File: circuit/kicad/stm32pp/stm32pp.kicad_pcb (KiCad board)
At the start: 2 copper layers, 59.8 x 34.2 mm, 30 parts, among them J1 USB_B_Micro, J2 USB_B_Micro, J3 Conn_01x04_Male, J4 Conn_01x08_Male, J5 Conn_01x08_Male, J6 Conn_01x08_Male, J7 Conn_01x08_Male, J8 Conn_01x02_Male, SW1 SW_Push, SW2 SW_Push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

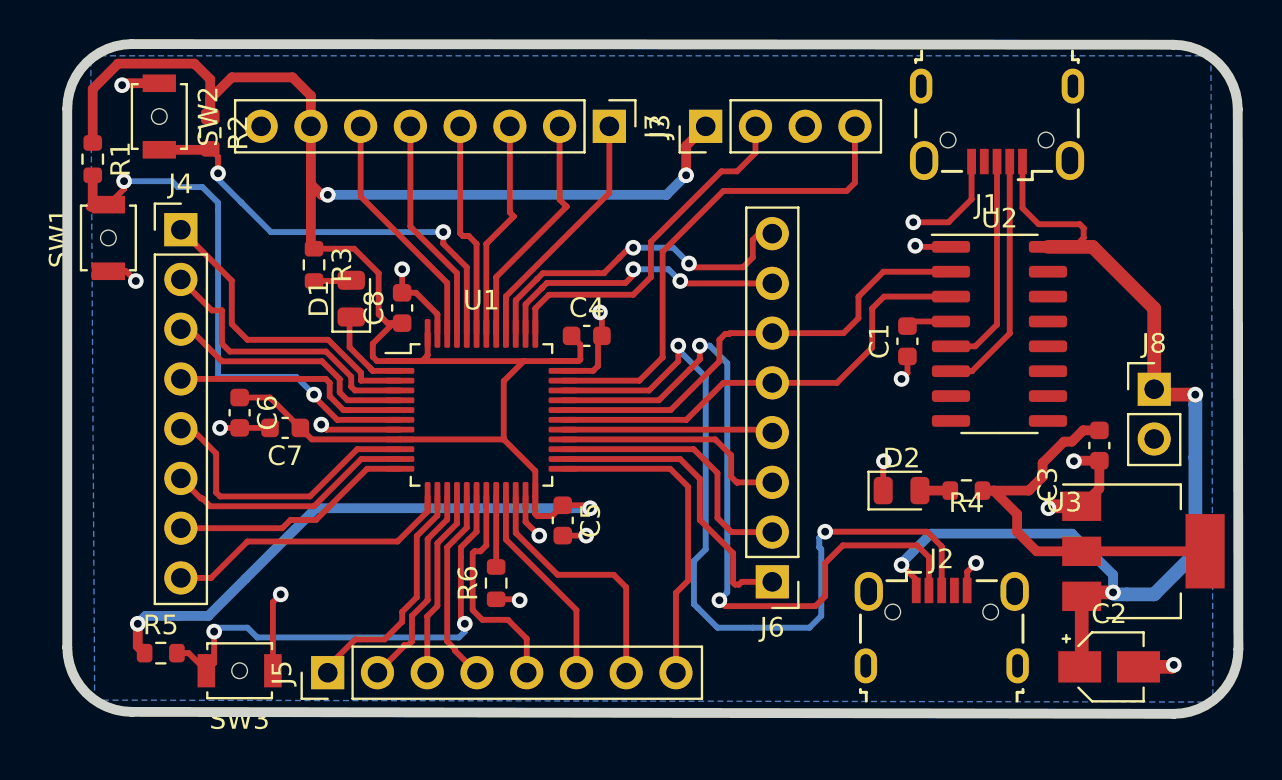
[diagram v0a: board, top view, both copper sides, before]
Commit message: STM32 PP
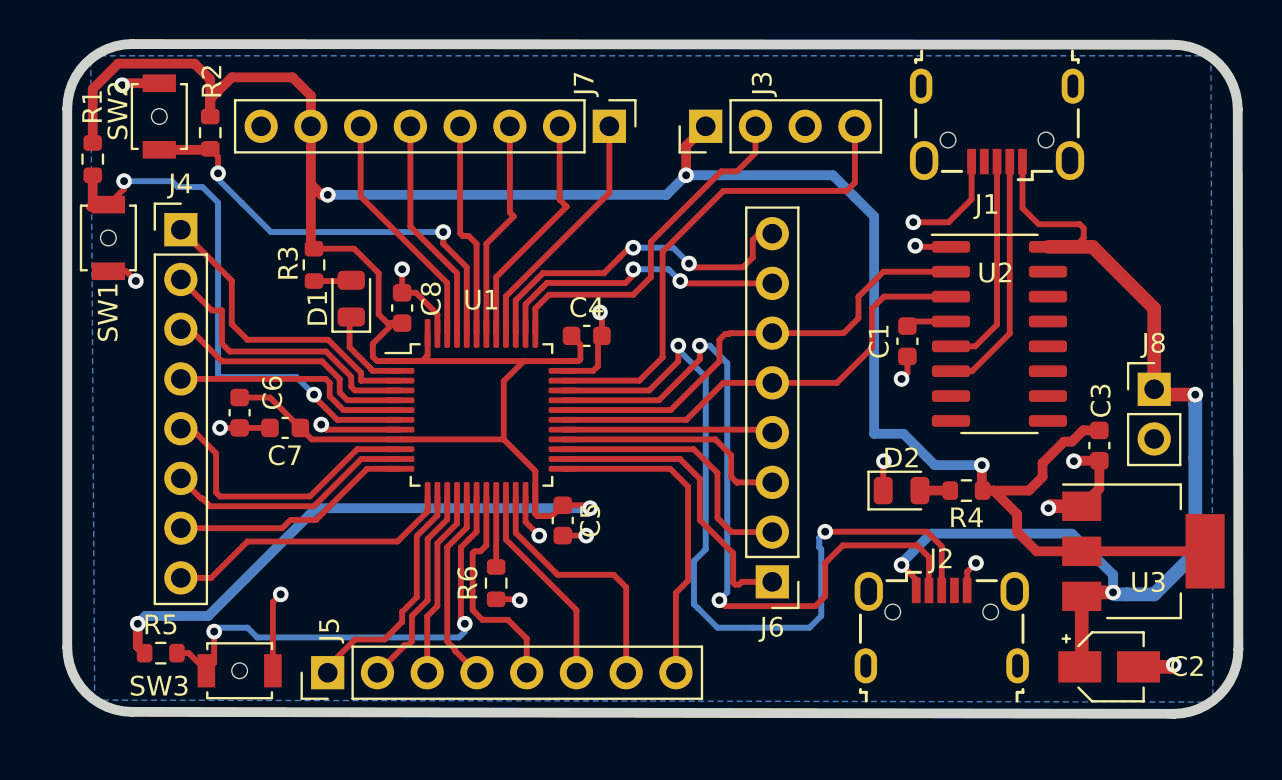
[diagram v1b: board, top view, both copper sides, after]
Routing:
- net +3.3V: track 146.6 -> 175.7 mm, vias 4 -> 5
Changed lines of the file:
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@@
     (property "Sheetname" "")
     (attr smd)
-    (fp_text reference "SW1" (at 0 -2.5 90) (layer "F.SilkS")
+    (fp_text reference "SW1" (at -3.8 0 90) (layer "F.SilkS")
       (effects (font (size 1 1) (thickness 0.15)))
     )
@@
     (property "Sheetname" "")
     (attr through_hole)
-    (fp_text reference "J7" (at 0 -2.33 90) (layer "F.SilkS")
+    (fp_text reference "J7" (at -2.2 1.28 90) (layer "F.SilkS")
       (effects (font (size 1 1) (thickness 0.15)))
     )
@@
     (property "Sheetname" "")
     (attr smd)
-    (fp_text reference "R3" (at 0 -1.43 90) (layer "F.SilkS")
+    (fp_text reference "R3" (at -0.075 1.3 90) (layer "F.SilkS")
       (effects (font (size 1 1) (thickness 0.15)))
     )
@@
     (property "Sheetname" "")
     (attr smd)
-    (fp_text reference "R2" (at 0 -1.43 90) (layer "F.SilkS")
+    (fp_text reference "R2" (at -2.625 -0.1 90) (layer "F.SilkS")
       (effects (font (size 1 1) (thickness 0.15)))
     )
@@
     (property "Sheetname" "")
     (attr smd)
-    (fp_text reference "C3" (at 2 2.6325 90) (layer "F.SilkS")
+    (fp_text reference "C3" (at -2.3 -0.1 90) (layer "F.SilkS")
       (effects (font (size 1 1) (thickness 0.15)))
     )
@@
     (pad "6" thru_hole oval (at 3.725 -1.85 180) (size 1.45 2) (drill oval 0.85 1.4) (layers *.Cu *.Mask)
       (net 1 "GND") (pinfunction "Shield") (pintype "passive"))
-    (model "${KICAD6_3DMODEL_DIR}/Connector_USB.3dshapes/USB_Micro-B_Wuerth_629105150521.wrl"
-      (offset (xyz 0 0 0))
-      (scale (xyz 1 1 1))
-      (rotate (xyz 0 0 0))
+    (model "${KIPRJMOD}/libs/pkg3d/molex_0473460001.stp"
+      (offset (xyz 0 -1.2 0))
+      (scale (xyz 1 1 1))
+      (rotate (xyz -90 0 0))
     )
   )
@@
     (property "Sheetname" "")
     (attr through_hole)
-    (fp_text reference "J3" (at 0 -2.33 90) (layer "F.SilkS")
+    (fp_text reference "J3" (at 2.2 2.9 90) (layer "F.SilkS")
       (effects (font (size 1 1) (thickness 0.15)))
     )
@@
     (property "Sheetname" "")
     (attr smd)
-    (fp_text reference "U3" (at -4.0625 -2.5) (layer "F.SilkS")
+    (fp_text reference "U3" (at 0.25 1.6) (layer "F.SilkS")
       (effects (font (size 1 1) (thickness 0.15)))
     )
@@
     (property "Sheetname" "")
     (attr smd)
-    (fp_text reference "R4" (at 0 -0.63) (layer "F.SilkS")
+    (fp_text reference "R4" (at 0 -1.4) (layer "F.SilkS")
       (effects (font (size 1 1) (thickness 0.15)))
     )
@@
     (property "Sheetname" "")
     (attr through_hole)
-    (fp_text reference "J5" (at 0 -2.33 90) (layer "F.SilkS")
+    (fp_text reference "J5" (at 2.2 0.1 90) (layer "F.SilkS")
       (effects (font (size 1 1) (thickness 0.15)))
     )
@@
     (property "Sheetname" "")
     (attr smd)
-    (fp_text reference "C2" (at 0 -2.7) (layer "F.SilkS")
+    (fp_text reference "C2" (at 4 0) (layer "F.SilkS")
       (effects (font (size 1 1) (thickness 0.15)))
     )
@@
     (property "Sheetname" "")
     (attr smd)
-    (fp_text reference "C6" (at 0 -1.43 90) (layer "F.SilkS")
+    (fp_text reference "C6" (at -1.025 -1.7 90) (layer "F.SilkS")
       (effects (font (size 1 1) (thickness 0.15)))
     )
@@
     (property "Sheetname" "")
     (attr smd)
-    (fp_text reference "U2" (at 0 -5.9) (layer "F.SilkS")
+    (fp_text reference "U2" (at -0.2 -3.1) (layer "F.SilkS")
       (effects (font (size 1 1) (thickness 0.15)))
     )
@@
     (pad "6" thru_hole oval (at -3.875 1.95) (size 1.15 1.8) (drill oval 0.55 1.2) (layers *.Cu *.Mask)
       (net 1 "GND") (pinfunction "Shield") (pintype "passive"))
-    (model "${KICAD6_3DMODEL_DIR}/Connector_USB.3dshapes/USB_Micro-B_Wuerth_629105150521.wrl"
-      (offset (xyz 0 0 0))
-      (scale (xyz 1 1 1))
-      (rotate (xyz 0 0 0))
+    (model "${KIPRJMOD}/libs/pkg3d/molex_0473460001.stp"
+      (offset (xyz 0 -1.2 0))
+      (scale (xyz 1 1 1))
+      (rotate (xyz -90 0 0))
     )
   )
@@
     (property "Sheetname" "")
     (attr smd)
-    (fp_text reference "SW3" (at 0 -2.5) (layer "F.SilkS")
+    (fp_text reference "SW3" (at 4.1 -0.8) (layer "F.SilkS")
       (effects (font (size 1 1) (thickness 0.15)))
     )
@@
     (property "Sheetname" "")
     (attr smd)
-    (fp_text reference "SW2" (at 0 -2.5 90) (layer "F.SilkS")
+    (fp_text reference "SW2" (at -0.3 2.1 90) (layer "F.SilkS")
       (effects (font (size 1 1) (thickness 0.15)))
     )
@@
     (property "Sheetname" "")
     (attr smd)
-    (fp_text reference "C8" (at 0 -1.43 90) (layer "F.SilkS")
+    (fp_text reference "C8" (at 0.475 1.5 90) (layer "F.SilkS")
       (effects (font (size 1 1) (thickness 0.15)))
     )
@@
     (property "Sheetname" "")
     (attr smd)
-    (fp_text reference "D1" (at 0 -1.65 90) (layer "F.SilkS")
+    (fp_text reference "D1" (at -0.5 -1.7 90) (layer "F.SilkS")
       (effects (font (size 1 1) (thickness 0.15)))
     )
@@
     (property "Sheetname" "")
     (attr smd)
-    (fp_text reference "R1" (at 0 -1.43 90) (layer "F.SilkS")
+    (fp_text reference "R1" (at -2.675 0 90) (layer "F.SilkS")
       (effects (font (size 1 1) (thickness 0.15)))
     )
@@
   (segment (start 139.4 82.064468) (end 139.4 81.4) (width 0.3) (layer "F.Cu") (net 4))
   (segment (start 127.4 95.7) (end 127.4 96.85) (width 0.5) (layer "F.Cu") (net 4))
+  (segment (start 170.5 87.6) (end 170.5 88.8625) (width 0.5) (layer "F.Cu") (net 4))
   (segment (start 139.623032 82.2875) (end 139.4 82.064468) (width 0.3) (layer "F.Cu") (net 4))
   (segment (start 140.7875 86.2875) (end 146.0875 86.2875) (width 0.3) (layer "F.Cu") (net 4))
@@
   (segment (start 147.1125 82.2875) (end 146.0875 83.3125) (width 0.3) (layer "F.Cu") (net 4))
   (segment (start 155.4 72.8) (end 155.4 71.3) (width 0.5) (layer "F.Cu") (net 4))
+  (segment (start 170.5 88.8625) (end 170.5375 88.9) (width 0.5) (layer "F.Cu") (net 4))
   (segment (start 148.55 90.2) (end 149.1 89.65) (width 0.3) (layer "F.Cu") (net 4))
   (segment (start 175.1 86.4) (end 174.7 86.4) (width 0.5) (layer "F.Cu") (net 4))
@@
   (via (at 155.4 72.8) (size 0.8) (drill 0.4) (layers "F.Cu" "B.Cu") (net 4))
   (via (at 150.5 89.8) (size 0.8) (drill 0.4) (layers "F.Cu" "B.Cu") (net 4))
+  (via (at 170.5 87.6) (size 0.8) (drill 0.4) (layers "F.Cu" "B.Cu") (net 4))
   (via (at 137.1 73.8) (size 0.8) (drill 0.4) (layers "F.Cu" "B.Cu") (net 4))
   (via (at 127.4 95.7) (size 0.8) (drill 0.4) (layers "F.Cu" "B.Cu") (net 4))
+  (segment (start 166.5 86) (end 167.7 87.2) (width 0.5) (layer "B.Cu") (net 4))
+  (segment (start 165 74.9) (end 165 86) (width 0.5) (layer "B.Cu") (net 4))
   (segment (start 129.5 95.3) (end 127.8 95.3) (width 0.5) (layer "B.Cu") (net 4))
   (segment (start 127.8 95.3) (end 127.4 95.7) (width 0.5) (layer "B.Cu") (net 4))
@@
   (segment (start 154.4 73.8) (end 155.4 72.8) (width 0.5) (layer "B.Cu") (net 4))
   (segment (start 137.1 73.8) (end 154.4 73.8) (width 0.5) (layer "B.Cu") (net 4))
+  (segment (start 165 86) (end 166.5 86) (width 0.5) (layer "B.Cu") (net 4))
   (segment (start 136.5 89.8) (end 132.9 93.4) (width 0.5) (layer "B.Cu") (net 4))
+  (segment (start 167.7 87.2) (end 168.1 87.6) (width 0.5) (layer "B.Cu") (net 4))
   (segment (start 132.9 93.4) (end 131 95.3) (width 0.5) (layer "B.Cu") (net 4))
+  (segment (start 155.4 72.8) (end 162.9 72.8) (width 0.5) (layer "B.Cu") (net 4))
+  (segment (start 162.9 72.8) (end 164 73.9) (width 0.5) (layer "B.Cu") (net 4))
+  (segment (start 164 73.9) (end 165 74.9) (width 0.5) (layer "B.Cu") (net 4))
   (segment (start 131 95.3) (end 129.5 95.3) (width 0.5) (layer "B.Cu") (net 4))
+  (segment (start 168.1 87.6) (end 170.5 87.6) (width 0.5) (layer "B.Cu") (net 4))
   (segment (start 138.214213 81.585787) (end 138.214213 80.123287) (width 0.3) (layer "F.Cu") (net 5))
   (segment (start 140.7875 82.7875) (end 139.3875 82.7875) (width 0.3) (layer "F.Cu") (net 5))
